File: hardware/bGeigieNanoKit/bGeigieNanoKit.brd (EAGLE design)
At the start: 96.2 x 66.7 mm, 33 parts, among them T1 2SC1815

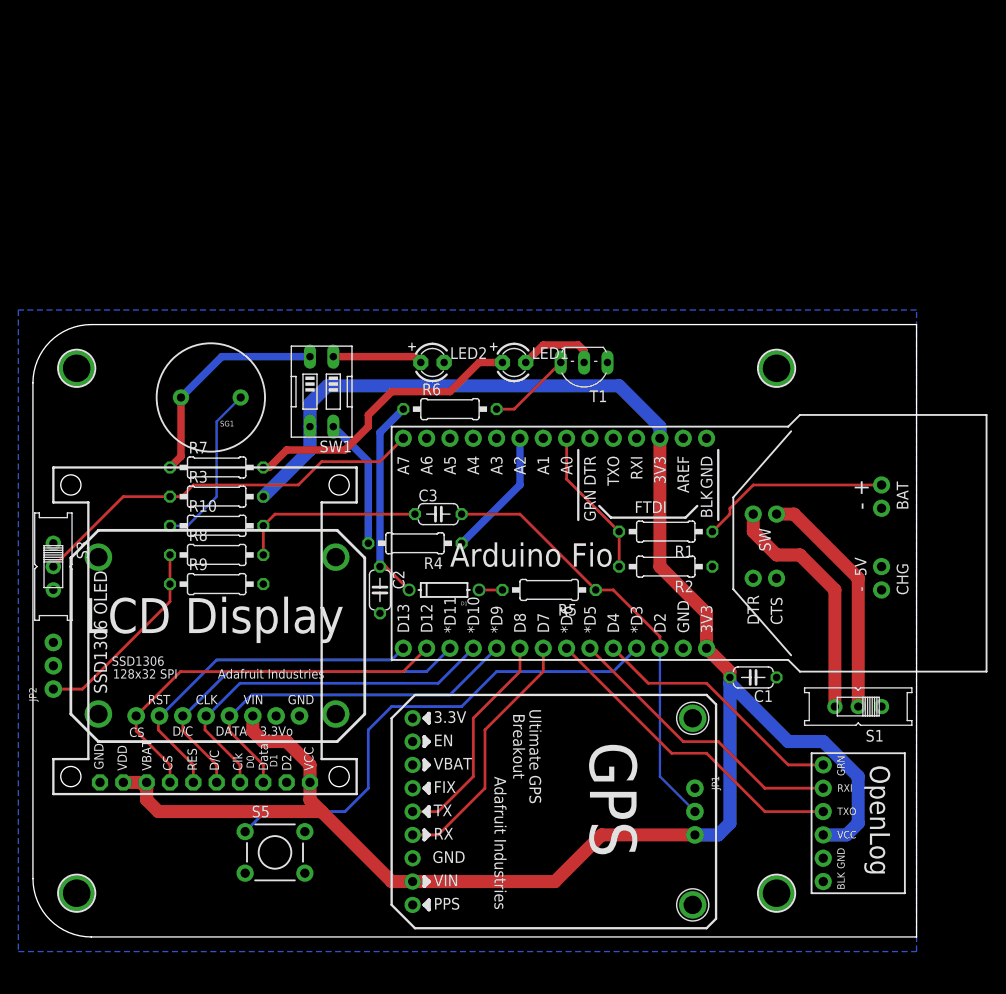
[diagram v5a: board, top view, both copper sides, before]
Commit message: cleaned up final routing
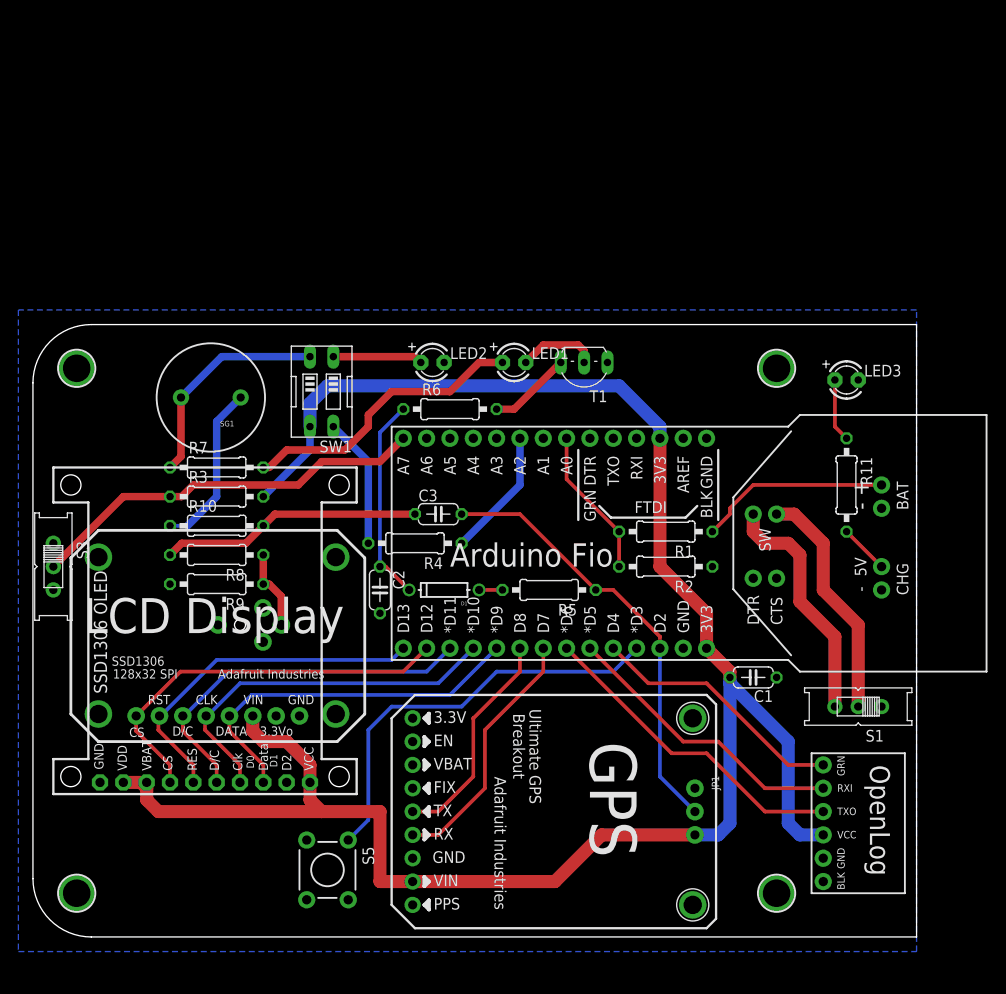
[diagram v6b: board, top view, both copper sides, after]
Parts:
- removed JP2: (no value), microbuilder:1X03_ROUND_76
- added LED3: RED, adafruit:LED3MM
- added R11: (no value), rcl:0207/10
- added U1: (no value), SparkFun:STEREOJACK2.5MM_STEREOJACK2.5MM
- moved S5 6.02 mm to (33.7, 8.89), turned to 270 degrees
- turned R8 to 180 degrees
- turned R9 to 180 degrees
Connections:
- new net N$29: LED3.A, R11.1
- net GND: now also LED3.K, U1.RING1, U1.RING2; no longer JP2.3
- net N$25: now also U1.TIP; no longer JP2.1
- net VIN: now also R11.2
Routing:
- net N$25: track 21.7 -> 8.80 mm
- net N$20: track 54.6 -> 45.8 mm
- net N$24: track 20.2 -> 28.5 mm
- net N$29: track 0.00 -> 6.88 mm
- net VIN: track 0.00 -> 5.39 mm
- net VCC: track 216.5 -> 215.5 mm

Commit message: cleaning up libs and updating brd
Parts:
- U$3: device open_hw_sockets:ULTIMATE_GPS_V3 -> open_hw_sockets:ULTIMATE_GPS_V3_TOP
- U$4: device open_hw_sockets:SSD1306_128X32_SPI_LCD -> open_hw_sockets:SSD1306_128X32_SPI_LCD_TOP
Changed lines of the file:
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@@
 </autorouter>
 <elements>
-<element name="U$4" library="open_hw_sockets" package="SSD1306_128X32_SPI_LCD" value="LCD" x="5.715" y="22.86"/>
-<element name="U$3" library="open_hw_sockets" package="ULTIMATE_GPS_V3" value="GPS" x="40.64" y="27.94" rot="R270"/>
+<element name="U$4" library="open_hw_sockets" package="SSD1306_128X32_SPI_LCD_TOP" value="LCD" x="5.715" y="22.86"/>
+<element name="U$3" library="open_hw_sockets" package="ULTIMATE_GPS_V3_TOP" value="GPS" x="40.64" y="27.94" rot="R270"/>
 <element name="LED1" library="adafruit" package="LED3MM" value="" x="53.975" y="64.135"/>
 <element name="LED2" library="adafruit" package="LED3MM" value="RED" x="45.085" y="64.135"/>

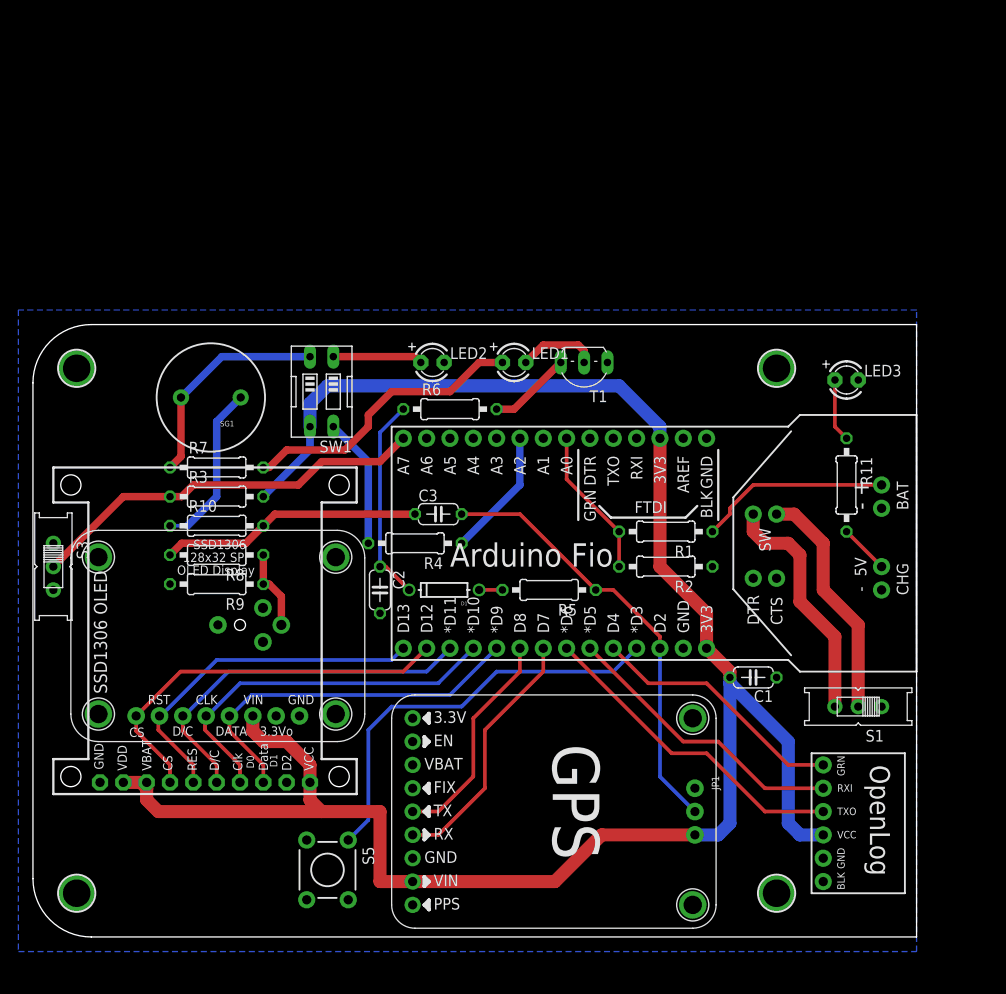
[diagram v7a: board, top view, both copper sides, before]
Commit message: smashing all parts and moving labels to be visable adding current limit resistor for charge led add lables to leds
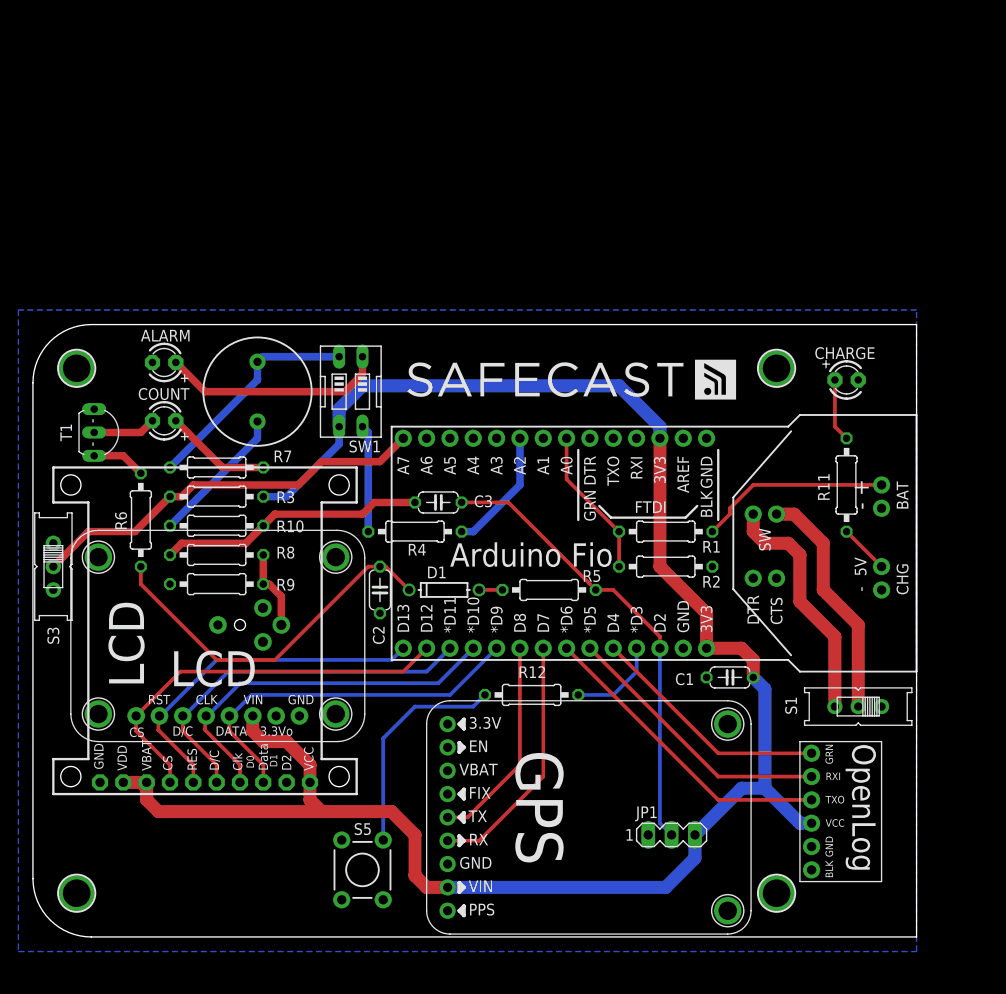
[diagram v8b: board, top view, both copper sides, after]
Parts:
- removed LED1: (no value), adafruit:LED3MM
- removed LED2: RED, adafruit:LED3MM
- added ALARM: RED, adafruit:LED3MM
- added COUNT: BLUE, adafruit:LED3MM
- added R12: 1k, rcl:0207/10
- added U$10: (no value), open_hw_sockets:SAFECAST_LOGO1
- C1, C2, C3: value (none) -> 0.1uF
- JP1: device microbuilder:1X03_ROUND_76 -> con-lstb:MA03-1
- R1: value (none) -> 9.1k
- R10, R11, R2, R4, R5, R9: value (none) -> 1k
- R3, R8: value (none) -> 47k
- R6: value (none) -> 100k
- R7: value (none) -> 51 Ohm
- SG1: value BUZZERPTH -> BUZZER
- U$1: value OPENLOG_MIN -> OPENLOG_MINITOP; device open_hw_sockets:OPENLOG_MIN -> open_hw_sockets:OPENLOG_TOP_MINI
- moved T1 53.9 mm to (8.26, 56.5), turned to 270 degrees
- moved R6 35.8 mm to (13.3, 47.0), turned to 90 degrees
- moved SG1 5.12 mm to (26.0, 61.0), turned to 90 degrees
- moved U$3 3.86 mm to (44.5, 27.3)
- moved S5 3.81 mm to (37.5, 8.89)
- moved JP1 3.59 mm to (71.1, 12.7), turned to 0 degrees
- moved SW1 3.17 mm to (36.2, 61.0)
- moved C1 2.54 mm to (77.5, 29.8), turned to 0 degrees
- moved U$1 1.80 mm to (85.1, 22.9)
- moved C3 1.27 mm to (45.7, 48.9)
- moved R4 1.27 mm to (43.2, 45.7)
- renumbered LED3 to CHARGE
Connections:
- new net N$30: R12.2, U$2.JP1$4
- net GND: now also ALARM.K; no longer LED2.K
- net N$16: now also ALARM.A; no longer LED2.A
- net N$19: now also COUNT.A; no longer LED1.A
- net N$20: now also R12.1; no longer U$2.JP1$4
- net N$22: now also COUNT.K; no longer LED1.K
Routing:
- net N$20: track 45.8 -> 24.1 mm
- net N$19: track 31.5 -> 11.6 mm
- net N$27: track 22.4 -> 39.8 mm
- net N$16: track 9.79 -> 24.3 mm
- net VCC: track 215.5 -> 204.8 mm
- net N$30: track 0.00 -> 9.94 mm
- net N$28: track 9.09 -> 5.87 mm
- net N$23: track 18.3 -> 15.3 mm
- net N$17: track 14.3 -> 11.7 mm
- net N$18: track 47.7 -> 49.8 mm
- net N$22: track 8.67 -> 6.88 mm
- net N$8: track 35.3 -> 33.5 mm
- net N$9: track 31.7 -> 29.9 mm
- net N$10: track 28.1 -> 26.3 mm
- net N$6: track 24.3 -> 22.9 mm
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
